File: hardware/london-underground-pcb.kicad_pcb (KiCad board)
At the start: 2 copper layers, 312 x 208 mm, 718 parts, among them SW1 TS-1187A-B-A-B, SW2 TS-1187A-B-A-B, SW3 TS-1187A-B-A-B, SW4 TS-1187A-B-A-B, U1 XIAO-RP2040-DIP

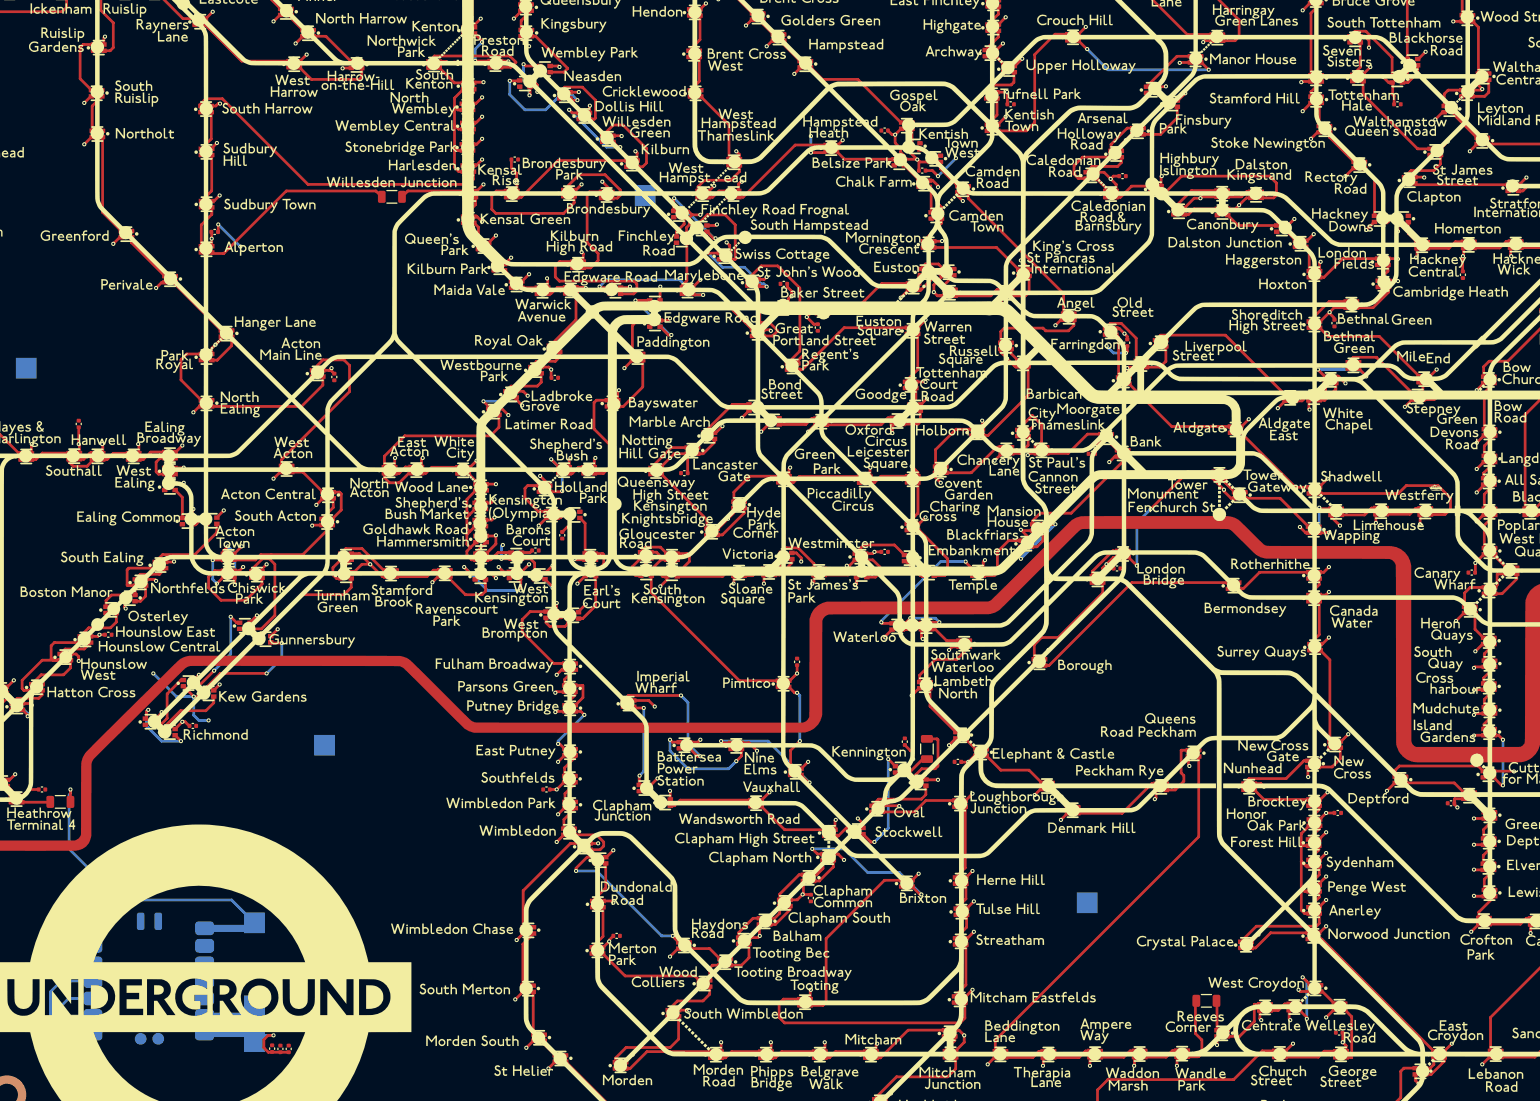
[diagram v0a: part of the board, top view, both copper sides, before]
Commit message: Fixed "unconnected items" in PCB viewer
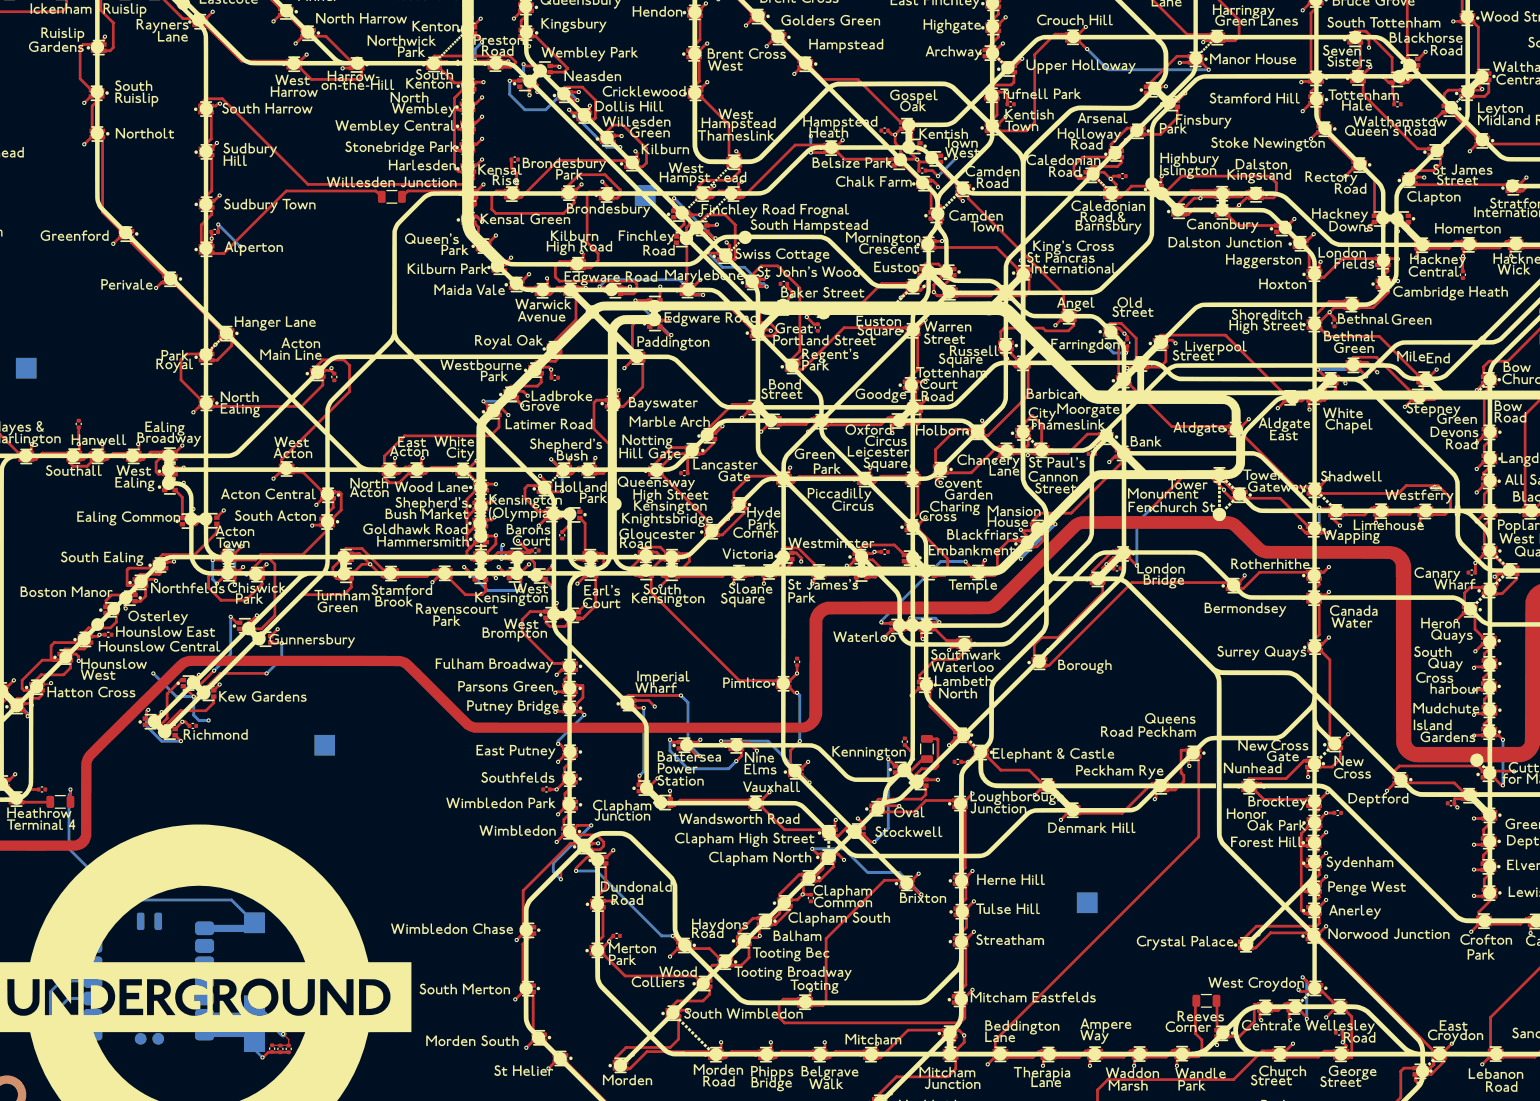
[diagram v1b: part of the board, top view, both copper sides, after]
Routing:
- net GND: track 304.6 -> 333.5 mm, vias 26 -> 29
- net +5V: track 1003.2 -> 1014.4 mm, vias 515 -> 523
